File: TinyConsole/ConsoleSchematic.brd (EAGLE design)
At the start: 100 x 80 mm, 8 parts, among them J1 POWER_JACKPTH, U1 JOYSTICKPTH, U2 TINY85-20-DIP

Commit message: Added actual files for TinyConsole.
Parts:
- moved JP1 4.02 mm to (44.5, 59.7)
- moved U2 4.02 mm to (26.7, 50.8)
- moved C2 4.02 mm to (5.08, 57.1), turned to 180 degrees
- moved C1 3.81 mm to (12.7, 57.1)
- moved U1 2.84 mm to (15.2, 27.9)
- moved R1 2.54 mm to (26.7, 61.0)
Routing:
- net N$1: track 79.7 -> 138.1 mm
- net GND: track 193.7 -> 144.2 mm
- net N$10: track 70.3 -> 29.2 mm
- net N$3: track 55.2 -> 22.6 mm
- net N$4: track 61.5 -> 40.0 mm
- net N$5: track 10.8 -> 17.8 mm
- net N$7: track 18.7 -> 25.1 mm
- net N$6: track 14.9 -> 21.0 mm
- net N$2: track 8.52 -> 6.54 mm

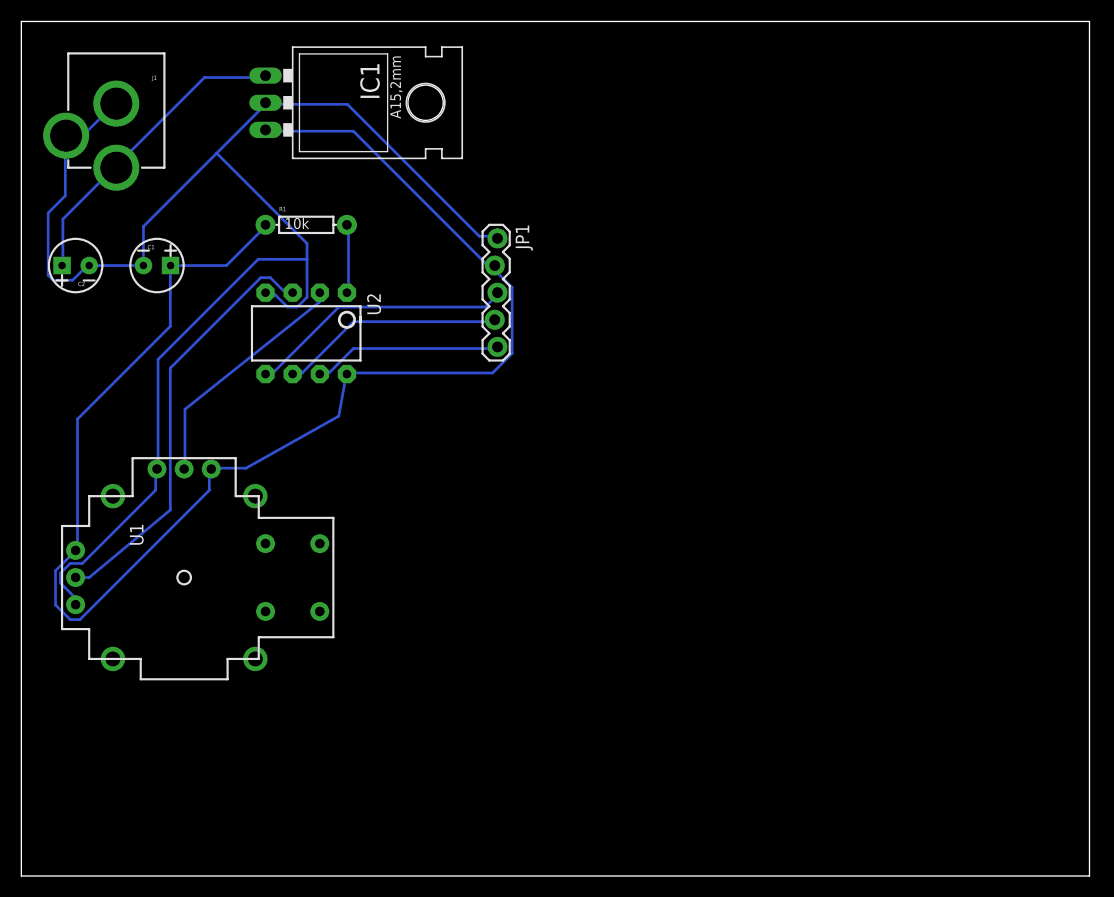
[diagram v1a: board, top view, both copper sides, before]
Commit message: TC: Updated PCB to use Ground Plane.
The ground plane is basically all the unused space on the PCB.  Since
the starting PCB is all copper, then we can use the ground plane as a
continuous wire.  This dramatically reduces the amount of nets needing
to be routed.
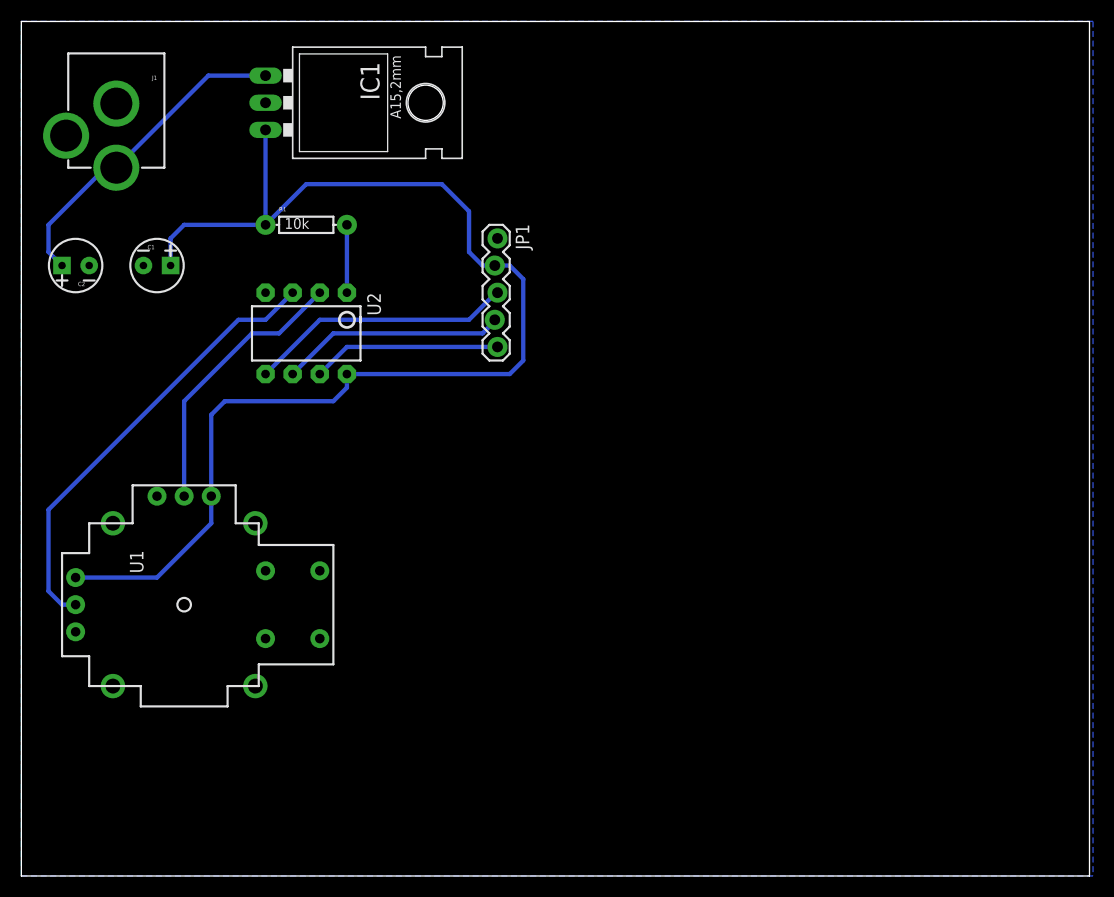
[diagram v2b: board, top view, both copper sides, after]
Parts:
- moved U1 2.54 mm to (15.2, 25.4)
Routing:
- net GND: track 144.2 -> 0.00 mm
- net N$1: track 138.1 -> 117.1 mm
- net N$3: track 22.6 -> 25.8 mm
- net N$4: track 40.0 -> 42.0 mm
- net N$10: track 29.2 -> 30.4 mm
- added copper zone on layer 16, net GND

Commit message: TinyConsole: Finished routing PCB.
I've now added an LED + Resistor, along with headers for the programmer.
I also checked the pin outs against the actual pin outs for the display
and I believe it now lines up correctly.  In short, I think it's good to
go!!!
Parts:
- removed JP1: (no value), SparkFun-Connectors:1X05_LOCK
- added D1: (no value), SparkFun-LED:LTE-302
- added DISPLAY, PROGRAMMER: (no value), SparkFun-Connectors:1X06
- added LEDRES: (no value), SparkFun-Passives:AXIAL-0.3EZ
- renumbered R1 to RESETRES
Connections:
- removed net N$5: JP1.5, U2.7
- removed net N$6: JP1.4, U2.6
- removed net N$7: JP1.3, U2.5
- new net CS: DISPLAY.4, PROGRAMMER.4, U2.6
- new net MOSI: DISPLAY.5, PROGRAMMER.5, U2.5
- new net SCK: DISPLAY.3, PROGRAMMER.3, U2.7
- new net VCC: C1.1, DISPLAY.1, IC1.OUT, LEDRES.P$2, PROGRAMMER.1, RESETRES.P$1, U1.H1, U1.V1, U2.8
- net GND: now also D1.C, DISPLAY.6, PROGRAMMER.6; no longer JP1.1
- net N$1: now also D1.A, LEDRES.P$1; no longer C1.1, IC1.OUT, JP1.2, RESETRES.P$1, U1.H1, U1.V1, U2.8
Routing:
- net VCC: track 0.00 -> 149.4 mm
- net N$1: track 117.1 -> 5.08 mm
- net MOSI: track 0.00 -> 32.6 mm
- net CS: track 0.00 -> 29.0 mm
- net N$7: track 24.9 -> 0.00 mm
- net SCK: track 0.00 -> 24.7 mm
- net N$6: track 21.1 -> 0.00 mm
- net N$5: track 17.7 -> 0.00 mm
- net GND: track 0.00 -> 10.2 mm
- net N$3: track 25.8 -> 26.5 mm

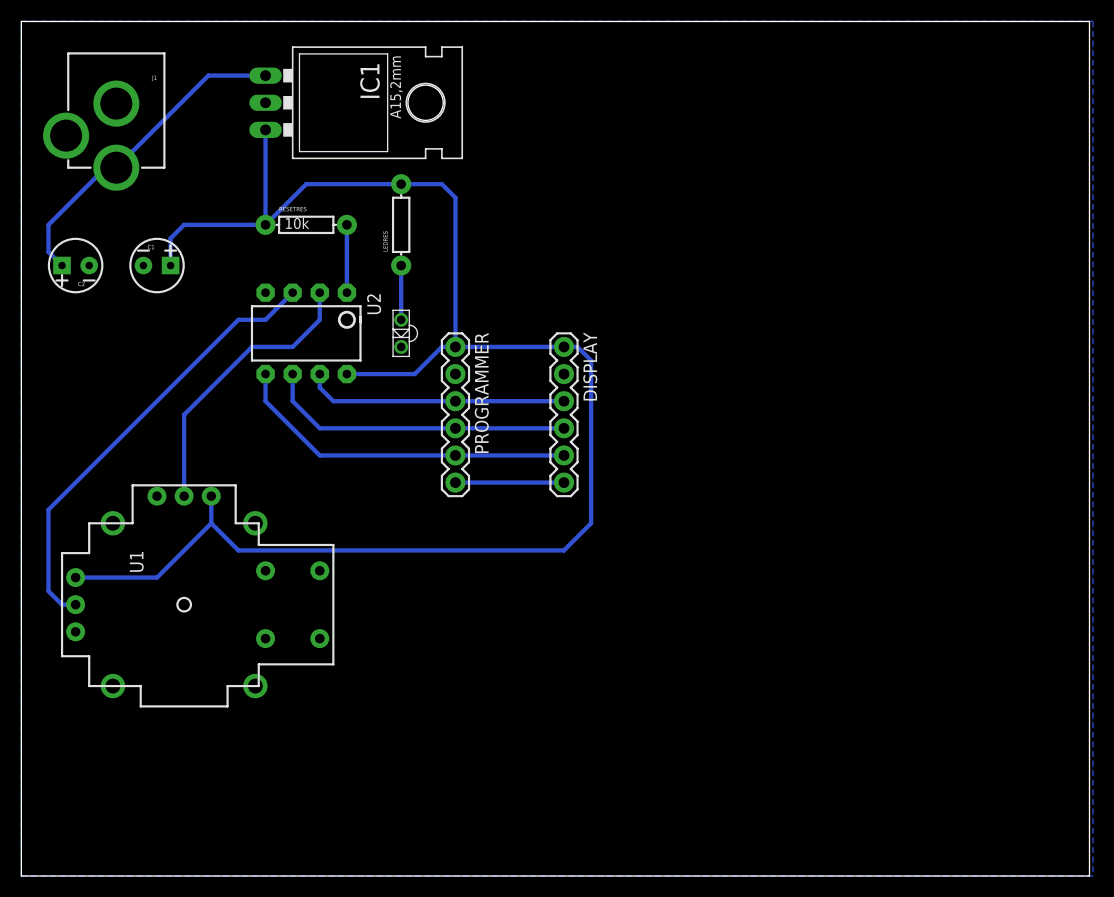
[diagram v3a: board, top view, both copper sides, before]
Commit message: TinyConsole: Minor tweaks before milling.
I adjusted the dimension of the board, and reduced the amount of copper
being filled in order to minimise problems with shorting the display.
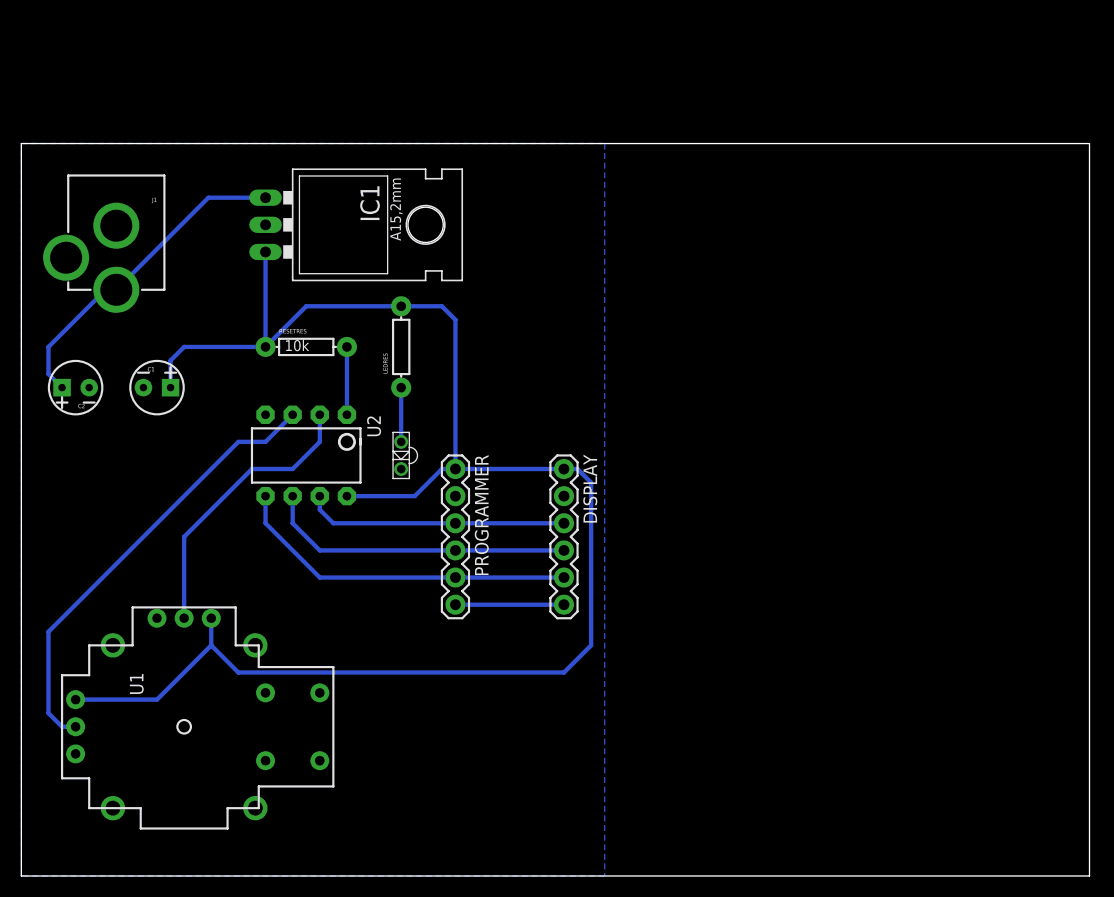
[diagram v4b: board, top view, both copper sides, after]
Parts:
- moved J1 11.4 mm to (8.89, 68.6)
- moved C1 11.4 mm to (12.7, 45.7)
- moved C2 11.4 mm to (5.08, 45.7)
- moved D1 11.4 mm to (35.6, 39.4)
- moved DISPLAY 11.4 mm to (50.8, 38.1)
- moved IC1 11.4 mm to (26.7, 61.0)
- moved LEDRES 11.4 mm to (35.6, 49.5)
- moved PROGRAMMER 11.4 mm to (40.6, 38.1)
- moved RESETRES 11.4 mm to (26.7, 49.5)
- moved U2 11.4 mm to (26.7, 39.4)
- moved U1 11.4 mm to (15.2, 14.0)
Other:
- board size 100 x 80 mm -> 100 x 68.6 mm
